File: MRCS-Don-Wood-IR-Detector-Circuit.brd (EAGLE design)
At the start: 85.1 x 33 mm, 21 parts, among them CON1 DC PWR, U1 LM324N

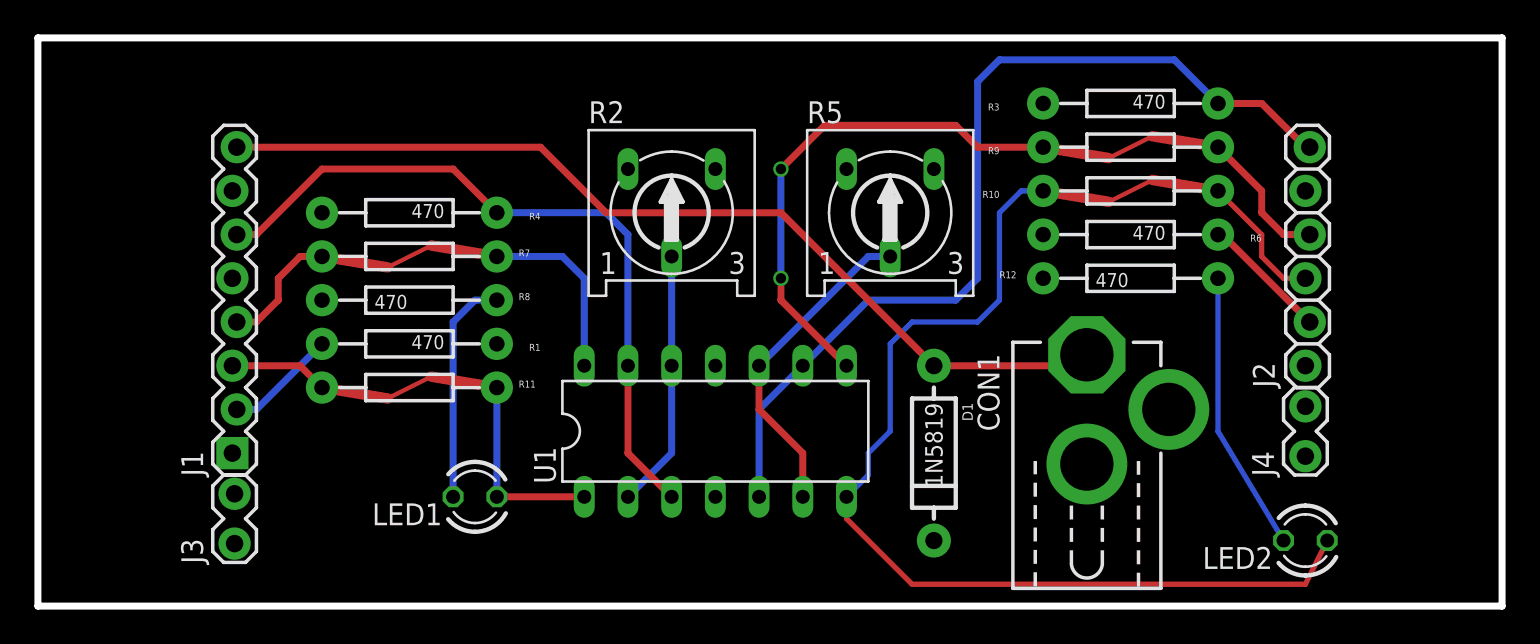
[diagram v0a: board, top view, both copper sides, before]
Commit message: moved the status LED to show illumination present
The LED now lights when the the illumination is present.  This is to help calibrate detection when using InfraRed illumination and reflected light set ups.
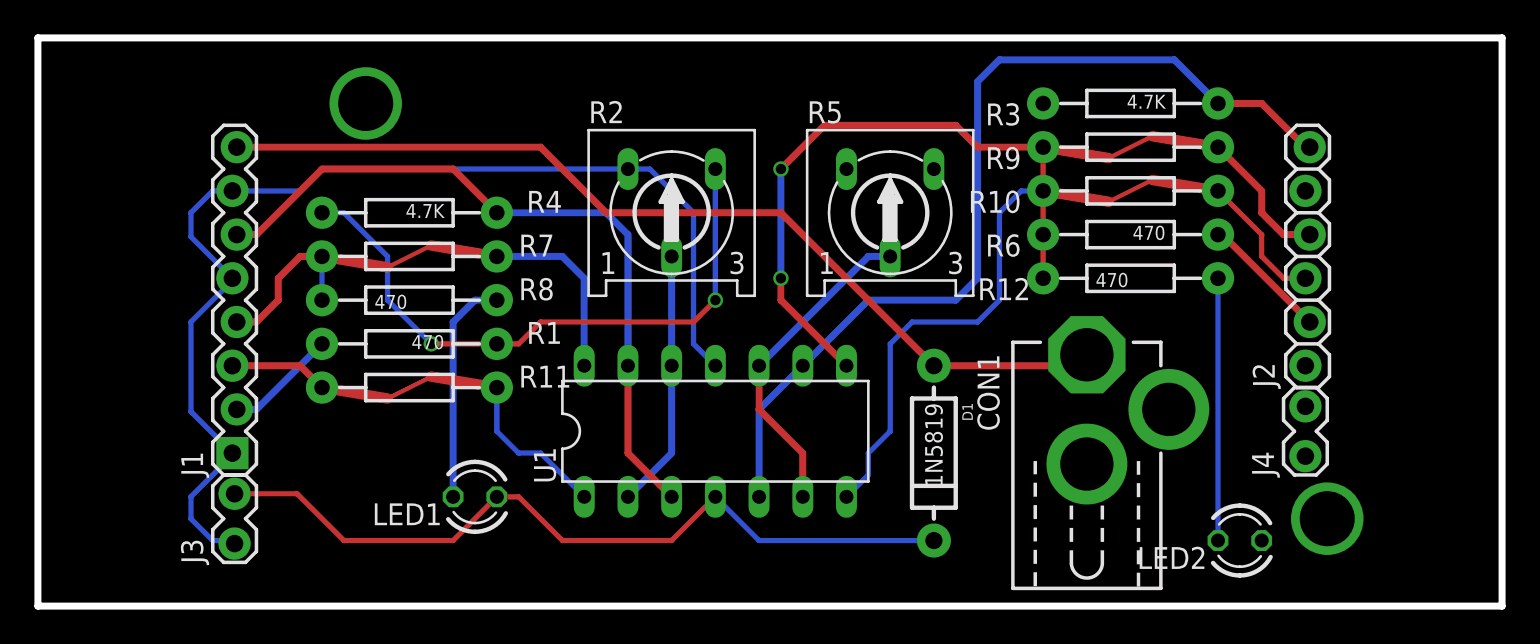
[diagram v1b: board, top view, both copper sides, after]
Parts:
- added U$1: (no value), MRCSLogoBtm:MRCSLOGOBTM
- added U$2: (no value), MRCSLogoTop:MRCSLOGOTOP
- added U$3: (no value), MRCS-prop65warningBtm:CA-PROP65WARNING
- R3, R4: value 470 -> 4.7K
- moved LED2 3.81 mm to (69.8, 3.81)
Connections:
- net GND: no longer R12.P$1, R8.P$1
- net N$10: now also R12.P$1
- net N$11: no longer LED2.A
- net N$13: no longer LED1.A
- net N$9: now also R8.P$1
- net VCC: now also LED1.A, LED2.A
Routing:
- net VCC: track 0.00 -> 82.2 mm, vias 0 -> 2
- net GND: track 0.00 -> 65.6 mm
- net N$11: track 57.8 -> 25.5 mm
- net N$10: track 29.8 -> 37.4 mm
- net N$9: track 10.7 -> 13.2 mm
- net N$13: track 11.4 -> 9.20 mm
- net N$1: track 16.3 -> 15.2 mm
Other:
- board text added: "+5 GND In 1 GND A1 B1 EM + EM - LED + LED -"
- board text added: "IN2 GND A2 B2 EM+ EM- LED+ LED-"
- board text added: "Optical Detector after Don Wood Seth Neumann 20201123"
- board text removed: "+5 GND In 1 GND A1 B1 LED + LED - LED + LED -"
- board text removed: "IN2 GND A2 B2 LED+ LED - LED+ LED -"
- board text removed: "Optical Detector after Don Wood Seth Neumann 20201028"
